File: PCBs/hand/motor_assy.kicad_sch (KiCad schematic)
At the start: 14 parts, among them J5 Conn_02x04_Odd_Even

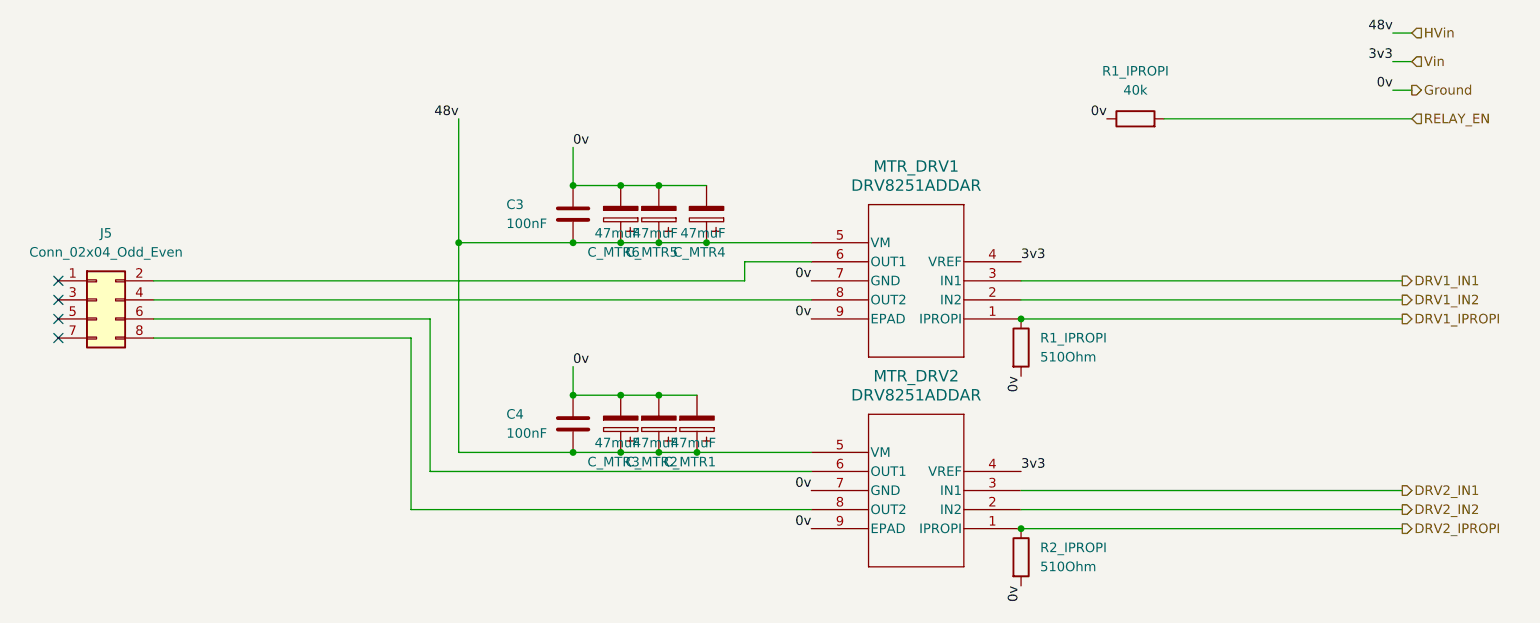
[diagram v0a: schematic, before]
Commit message: Updated ign with ever more variations of autosaves. Finished tracing hand, probably need new footprint for encoders. Next up: find footprints, redo IMU board
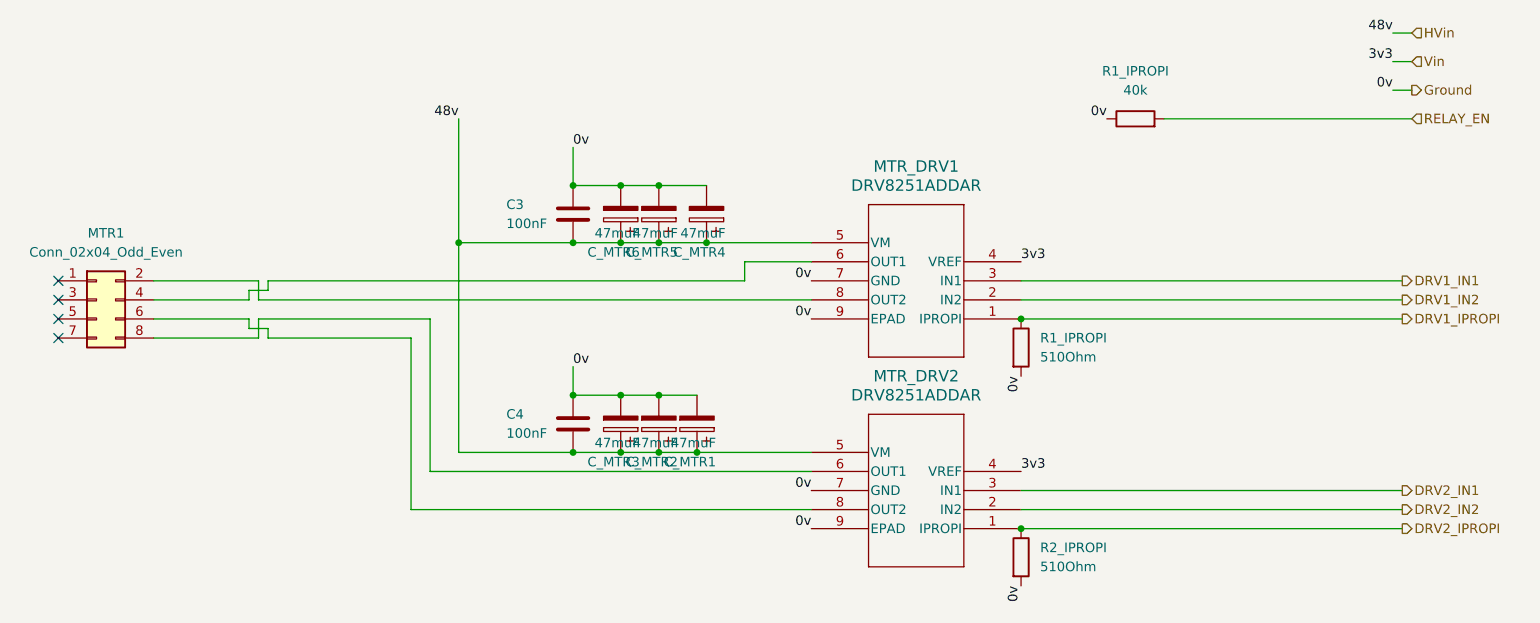
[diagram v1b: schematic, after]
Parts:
- MTR1: renamed from J5; footprint Connector_PinHeader_2.54mm:PinHeader_2x04_P2.54mm_Horizontal -> Connector_PinHeader_2.54mm:PinHeader_2x04_P2.54mm_Vertical
- R1_IPROPI: footprint Resistor_SMD:R_0805_2012Metric -> Resistor_SMD:R_0402_1005Metric
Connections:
- net at MTR_DRV2.6 (OUT1): now also MTR1.8 (Pin_8); no longer MTR1.6 (Pin_6)
- net at MTR_DRV2.8 (OUT2): now also MTR1.6 (Pin_6); no longer MTR1.8 (Pin_8)
- net at MTR_DRV1.6 (OUT1): now also MTR1.4 (Pin_4); no longer MTR1.2 (Pin_2)
- net at MTR_DRV1.8 (OUT2): now also MTR1.2 (Pin_2); no longer MTR1.4 (Pin_4)
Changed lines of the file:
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@@
   (no_connect (at 35.56 104.14))
   (no_connect (at 35.56 106.68))
+  (wire (pts (xy 48.26 109.22) (xy 62.23 109.22))
+    (stroke (width 0) (type default))
+  )
+  (wire (pts (xy 48.26 104.14) (xy 60.96 104.14))
+    (stroke (width 0) (type default))
+  )
   (wire (pts (xy 82.55 109.22) (xy 82.55 132.08))
     (stroke (width 0) (type default))
@@
     (stroke (width 0) (type default))
   )
-  (wire (pts (xy 48.26 101.6) (xy 127 101.6))
+  (wire (pts (xy 62.23 109.22) (xy 62.23 106.68))
     (stroke (width 0) (type default))
   )
@@
     (stroke (width 0) (type default))
   )
+  (wire (pts (xy 63.5 109.22) (xy 63.5 107.95))
+    (stroke (width 0) (type default))
+  )
   (wire (pts (xy 115.57 124.46) (xy 120.65 124.46))
     (stroke (width 0) (type default))
   )
+  (wire (pts (xy 60.96 104.14) (xy 60.96 102.87))
+    (stroke (width 0) (type default))
+  )
   (wire (pts (xy 120.65 124.46) (xy 135.89 124.46))
     (stroke (width 0) (type default))
@@
     (stroke (width 0) (type default))
   )
+  (wire (pts (xy 60.96 102.87) (xy 63.5 102.87))
+    (stroke (width 0) (type default))
+  )
   (wire (pts (xy 110.49 88.9) (xy 115.57 88.9))
     (stroke (width 0) (type default))
   )
-  (wire (pts (xy 48.26 106.68) (xy 85.09 106.68))
+  (wire (pts (xy 82.55 109.22) (xy 63.5 109.22))
     (stroke (width 0) (type default))
   )
@@
     (stroke (width 0) (type default))
   )
+  (wire (pts (xy 48.26 101.6) (xy 62.23 101.6))
+    (stroke (width 0) (type default))
+  )
+  (wire (pts (xy 62.23 104.14) (xy 135.89 104.14))
+    (stroke (width 0) (type default))
+  )
+  (wire (pts (xy 63.5 107.95) (xy 60.96 107.95))
+    (stroke (width 0) (type default))
+  )
   (wire (pts (xy 127 101.6) (xy 127 99.06))
     (stroke (width 0) (type default))
@@
     (stroke (width 0) (type default))
   )
-  (wire (pts (xy 48.26 104.14) (xy 135.89 104.14))
-    (stroke (width 0) (type default))
-  )
   (wire (pts (xy 85.09 106.68) (xy 85.09 127))
     (stroke (width 0) (type default))
   )
+  (wire (pts (xy 60.96 107.95) (xy 60.96 106.68))
+    (stroke (width 0) (type default))
+  )
   (wire (pts (xy 163.83 132.08) (xy 214.63 132.08))
     (stroke (width 0) (type default))
   )
+  (wire (pts (xy 62.23 101.6) (xy 62.23 104.14))
+    (stroke (width 0) (type default))
+  )
+  (wire (pts (xy 63.5 102.87) (xy 63.5 101.6))
+    (stroke (width 0) (type default))
+  )
+  (wire (pts (xy 63.5 101.6) (xy 127 101.6))
+    (stroke (width 0) (type default))
+  )
+  (wire (pts (xy 62.23 106.68) (xy 85.09 106.68))
+    (stroke (width 0) (type default))
+  )
   (wire (pts (xy 213.36 72.39) (xy 215.9 72.39))
     (stroke (width 0) (type default))
@@
     (stroke (width 0) (type default))
   )
-  (wire (pts (xy 48.26 109.22) (xy 82.55 109.22))
+  (wire (pts (xy 60.96 106.68) (xy 48.26 106.68))
     (stroke (width 0) (type default))
   )
@@
   )
   (symbol (lib_id "Connector_Generic:Conn_02x04_Odd_Even") (at 40.64 104.14 0) (unit 1)
-    (in_bom yes) (on_board yes) (dnp no) (fields_autoplaced)
-    (property "Reference" "J5" (at 41.91 95.25 0)
+    (in_bom yes) (on_board yes) (dnp no)
+    (property "Reference" "MTR1" (at 41.91 95.25 0)
       (effects (font (size 1.27 1.27)))
     )
@@
       (effects (font (size 1.27 1.27)))
     )
-    (property "Footprint" "Connector_PinHeader_2.54mm:PinHeader_2x04_P2.54mm_Horizontal" (at 40.64 104.14 0)
+    (property "Footprint" "Connector_PinHeader_2.54mm:PinHeader_2x04_P2.54mm_Vertical" (at 40.64 104.14 0)
       (effects (font (size 1.27 1.27)) hide)
     )
@@
       (project "hand"
         (path "/5df167e9-440d-40dc-8690-43ffe4e4c50d/710f463d-d939-4835-b806-0bed34cabba5"
-          (reference "J5") (unit 1)
+          (reference "MTR1") (unit 1)
         )
       )
@@
       (effects (font (size 1.27 1.27)))
     )
-    (property "Footprint" "Resistor_SMD:R_0805_2012Metric" (at 179.07 81.788 90)
-      (effects (font (size 1.27 1.27)) hide)
-    )
+    (property "Footprint" "Resistor_SMD:R_0402_1005Metric" (at 179.07 81.788 90)
+      (effects (font (size 1.27 1.27)) hide)
+    )

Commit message: Added pcb pdfs
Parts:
- renumbered C3 to C13, C4 to C14, R1_IPROPI to R_EN1, R1_IPROPI to R_IPROPI1, R2_IPROPI to R_IPROPI2
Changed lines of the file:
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@@
   (symbol (lib_id "Device:R") (at 163.83 138.43 0) (unit 1)
     (in_bom yes) (on_board yes) (dnp no) (fields_autoplaced)
-    (property "Reference" "R2_IPROPI" (at 166.37 137.16 0)
+    (property "Reference" "R_IPROPI2" (at 166.37 137.16 0)
       (effects (font (size 1.27 1.27)) (justify left))
     )
@@
     (instances
       (project "hand"
-        (path "/5df167e9-440d-40dc-8690-43ffe4e4c50d"
-          (reference "R2_IPROPI") (unit 1)
-        )
         (path "/5df167e9-440d-40dc-8690-43ffe4e4c50d/710f463d-d939-4835-b806-0bed34cabba5"
           (reference "R_IPROPI2") (unit 1)
@@
   (symbol (lib_id "Device:C") (at 104.14 92.71 0) (unit 1)
     (in_bom yes) (on_board yes) (dnp no)
-    (property "Reference" "C3" (at 95.25 91.44 0)
+    (property "Reference" "C13" (at 95.25 91.44 0)
       (effects (font (size 1.27 1.27)) (justify left))
     )
@@
     (instances
       (project "hand"
-        (path "/5df167e9-440d-40dc-8690-43ffe4e4c50d"
-          (reference "C3") (unit 1)
-        )
         (path "/5df167e9-440d-40dc-8690-43ffe4e4c50d/710f463d-d939-4835-b806-0bed34cabba5"
           (reference "C13") (unit 1)
@@
   (symbol (lib_id "Device:R") (at 179.07 80.01 90) (unit 1)
     (in_bom yes) (on_board yes) (dnp no) (fields_autoplaced)
-    (property "Reference" "R1_IPROPI" (at 179.07 73.66 90)
+    (property "Reference" "R_EN1" (at 179.07 73.66 90)
       (effects (font (size 1.27 1.27)))
     )
@@
     (instances
       (project "hand"
-        (path "/5df167e9-440d-40dc-8690-43ffe4e4c50d"
-          (reference "R1_IPROPI") (unit 1)
-        )
         (path "/5df167e9-440d-40dc-8690-43ffe4e4c50d/710f463d-d939-4835-b806-0bed34cabba5"
           (reference "R_EN1") (unit 1)
@@
   (symbol (lib_id "Device:C") (at 104.14 120.65 0) (unit 1)
     (in_bom yes) (on_board yes) (dnp no)
-    (property "Reference" "C4" (at 95.25 119.38 0)
+    (property "Reference" "C14" (at 95.25 119.38 0)
       (effects (font (size 1.27 1.27)) (justify left))
     )
@@
     (instances
       (project "hand"
-        (path "/5df167e9-440d-40dc-8690-43ffe4e4c50d"
-          (reference "C4") (unit 1)
-        )
         (path "/5df167e9-440d-40dc-8690-43ffe4e4c50d/710f463d-d939-4835-b806-0bed34cabba5"
           (reference "C14") (unit 1)
@@
   (symbol (lib_id "Device:R") (at 163.83 110.49 0) (unit 1)
     (in_bom yes) (on_board yes) (dnp no) (fields_autoplaced)
-    (property "Reference" "R1_IPROPI" (at 166.37 109.22 0)
+    (property "Reference" "R_IPROPI1" (at 166.37 109.22 0)
       (effects (font (size 1.27 1.27)) (justify left))
     )
@@
     (instances
       (project "hand"
-        (path "/5df167e9-440d-40dc-8690-43ffe4e4c50d"
-          (reference "R1_IPROPI") (unit 1)
-        )
         (path "/5df167e9-440d-40dc-8690-43ffe4e4c50d/710f463d-d939-4835-b806-0bed34cabba5"
           (reference "R_IPROPI1") (unit 1)
